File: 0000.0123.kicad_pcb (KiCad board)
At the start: 2 copper layers, 110 x 70 mm, 96 parts, among them J1 Conn_02x08_Odd_Even, J6 Conn_01x08, U1 TPA3255, U2 TL072, U3 TL072

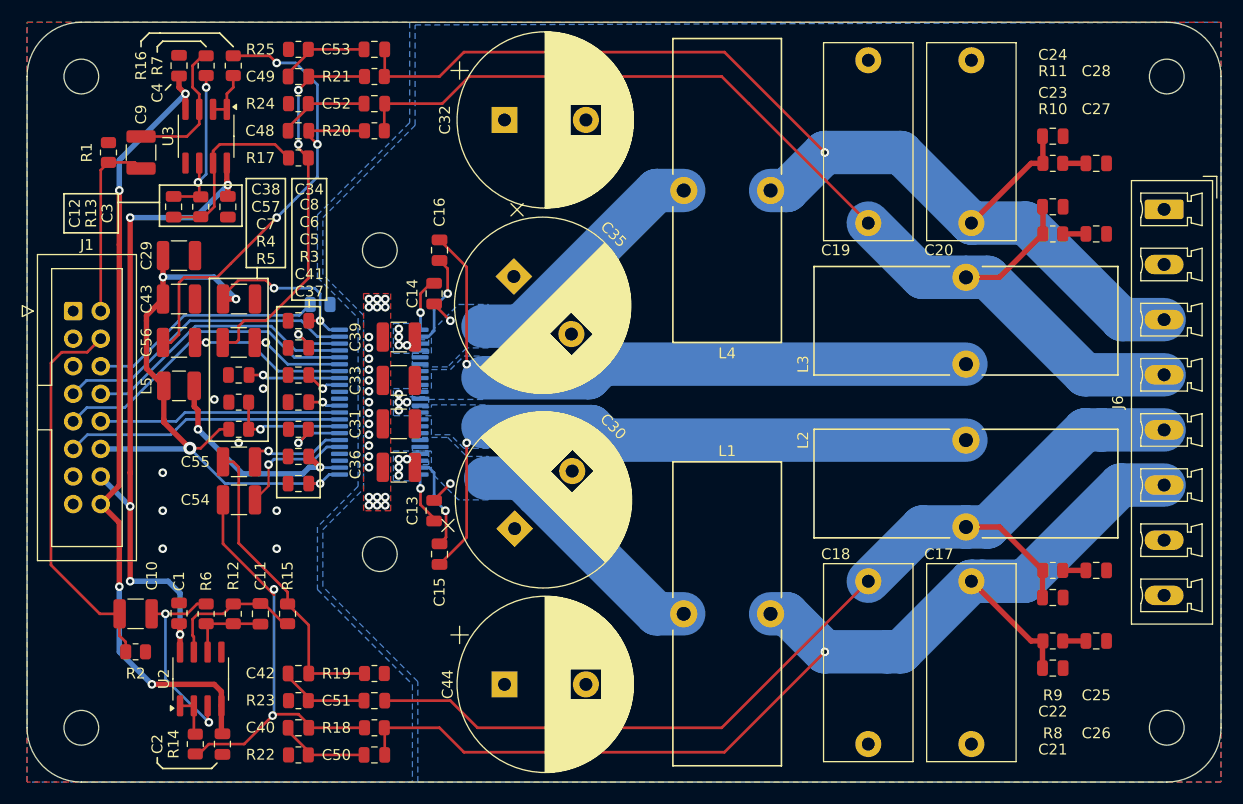
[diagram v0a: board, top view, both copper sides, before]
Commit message: Updated PCB layout.
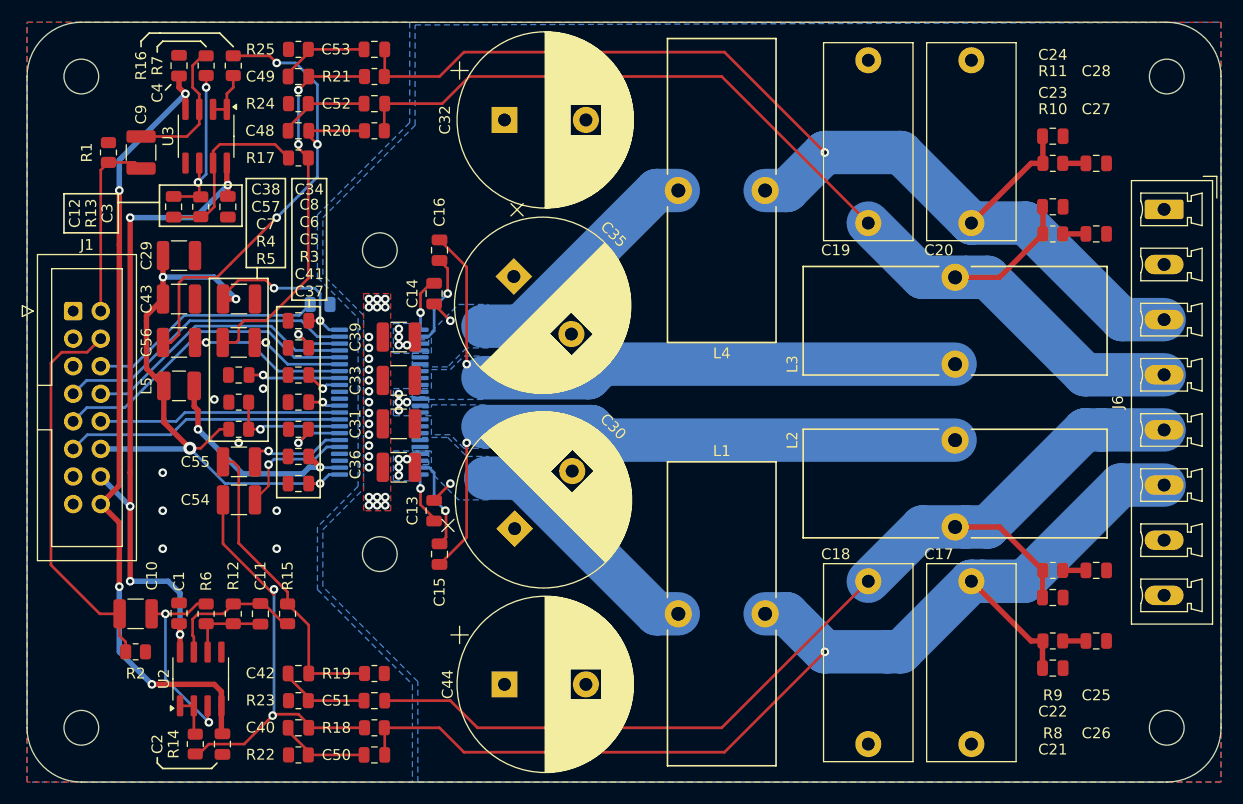
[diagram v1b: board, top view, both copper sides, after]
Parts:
- moved L2 1.00 mm to (195.5, 102.5)
- moved L3 1.00 mm to (195.5, 87.5)
- moved L1 0.50 mm to (174.0, 114.5)
- moved L4 0.50 mm to (174.0, 75.5)
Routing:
- net Net-(U1-OUT_C): track 57.5 -> 56.5 mm
- net Net-(U1-OUT_B): track 57.3 -> 56.3 mm
- net Net-(C14-Pad2): track 25.8 -> 25.3 mm
- net Net-(C13-Pad2): track 25.6 -> 25.1 mm
- net /CH2-: track 103.3 -> 103.8 mm
- net /CH1+: track 103.5 -> 104.0 mm

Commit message: Fixed minor error - R5 is now connected to +12V1 instead of +12V.
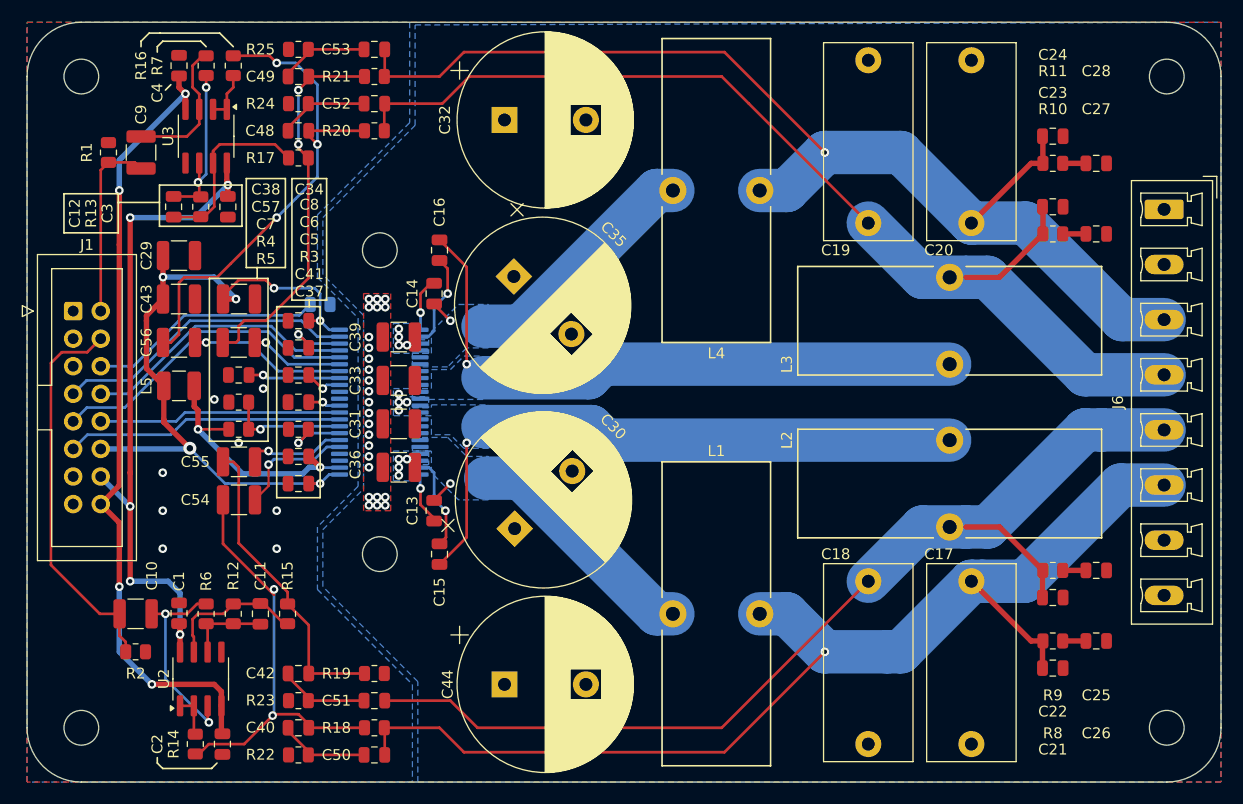
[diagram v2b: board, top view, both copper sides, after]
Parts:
- J1: value Conn_02x08_Odd_Even -> BH254
- moved L1 0.50 mm to (173.5, 114.5)
- moved L2 0.50 mm to (195.0, 102.5)
- moved L3 0.50 mm to (195.0, 87.5)
- moved L4 0.50 mm to (173.5, 75.5)
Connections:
- C41 pad 1: /+12V1 -> +12V1
- L5 pad 2: /+12V1 -> +12V1
- R5 pad 2: +12V -> +12V1
- U1 pad 2: /+12V1 -> +12V1
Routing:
- net +12V1: track 0.00 -> 23.4 mm, vias 0 -> 2
- net /+12V1: track 20.6 -> 0.00 mm, vias 2 -> 0
- net +12V: track 74.7 -> 70.4 mm
- net Net-(U1-OUT_C): track 56.5 -> 56.0 mm
- net Net-(U1-OUT_B): track 56.3 -> 55.8 mm
- net Net-(C14-Pad2): track 25.3 -> 24.8 mm
- net Net-(C13-Pad2): track 25.1 -> 24.6 mm
- net /CH2-: track 103.8 -> 104.3 mm
- net /CH1+: track 104.0 -> 104.5 mm

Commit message: Fixed some whoopsies.
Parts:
- C54, C55, C56, C57: footprint Capacitor_SMD:C_1210_3225Metric -> Capacitor_SMD:C_0805_2012Metric
- moved L5 4.00 mm to (124.0, 97.5)
- moved C54 1.50 mm to (129.5, 102.5)
- moved C55 0.50 mm to (129.5, 100.0)
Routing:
- net /CH1-: track 95.5 -> 99.5 mm
- net +12V1: track 23.4 -> 21.4 mm
- net /CH2+: track 98.0 -> 99.5 mm
- net +12V: track 70.4 -> 69.5 mm
- net Net-(C40-Pad1): track 40.2 -> 41.0 mm
- net Net-(C49-Pad1): track 35.6 -> 34.9 mm
- net Net-(C48-Pad1): track 47.4 -> 46.8 mm
- net /IN_CH1+: track 11.0 -> 10.4 mm
- net GND: vias 20 -> 21
